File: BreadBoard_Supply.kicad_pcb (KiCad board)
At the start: 2 copper layers, 19 parts, among them J1 Barrel_Jack_Switch, J2 Selector, J3 Conn_02x02_Odd_Even, J4 Conn_02x02_Odd_Even, U1 AMS1117-5.0, U2 AMS1117-3.3

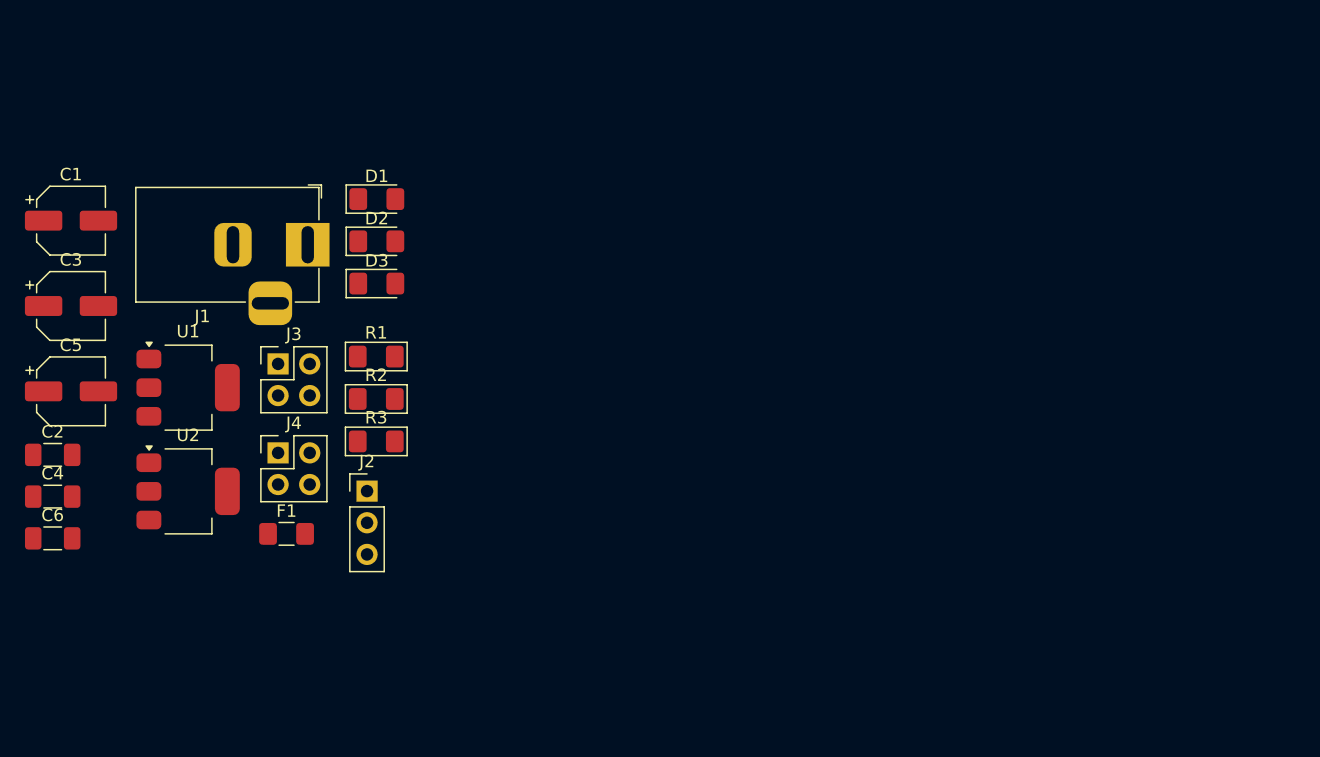
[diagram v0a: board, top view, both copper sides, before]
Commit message: Completed with DC input
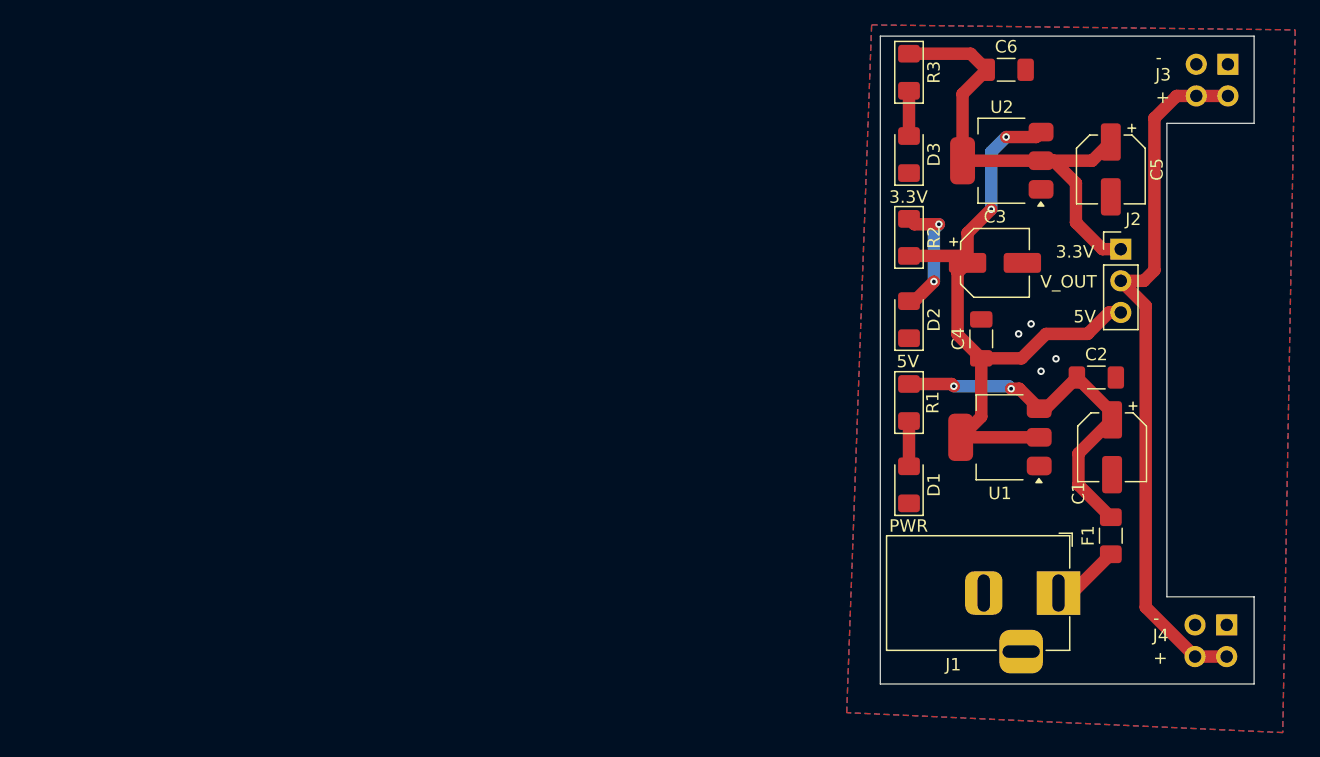
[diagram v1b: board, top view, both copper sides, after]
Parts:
- added REF**: KiCad-Logo2_5mm_SilkScreen, Symbol:KiCad-Logo2_5mm_SilkScreen, B.Cu at (205.4, 66.4)
- J3, J4: moved to B.Cu
- moved C1 85.5 mm to (211.3, 95.9), turned to -90 degrees
- moved C5 85.3 mm to (211.2, 73.6), turned to -90 degrees
- moved C6 85.3 mm to (202.8, 65.6)
- moved C2 84.0 mm to (210.0, 90.3)
- moved J3 79.9 mm to (220.6, 65.2), turned to 180 degrees
- moved J4 77.4 mm to (220.5, 110.2), turned to 180 degrees
- moved C4 75.6 mm to (200.8, 87.2), turned to 90 degrees
- moved C3 74.2 mm to (201.9, 81.1)
- moved U2 70.5 mm to (202.4, 72.9), turned to 180 degrees
- moved J1 66.4 mm to (207.0, 107.6)
- moved F1 66.2 mm to (211.2, 103.0), turned to 90 degrees
- moved U1 65.3 mm to (202.3, 95.1), turned to 180 degrees
- moved J2 63.5 mm to (212.0, 80.0)
- moved R3 52.0 mm to (195.0, 65.8), turned to -90 degrees
- moved D1 48.5 mm to (195.0, 98.9), turned to 90 degrees
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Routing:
- net /V_OUT: track 0.00 -> 57.1 mm
- net /5V: track 0.00 -> 54.1 mm, vias 0 -> 2
- net /3.3V: track 0.00 -> 38.6 mm
- net Net-(U1-VI): track 0.00 -> 29.9 mm, vias 0 -> 2
- net Net-(D2-A): track 0.00 -> 10.00 mm, vias 0 -> 2
- net Net-(F1-Pad1): track 0.00 -> 5.49 mm
- net Net-(D3-A): track 0.00 -> 3.63 mm
- net Net-(D1-A): track 0.00 -> 3.63 mm
- net GND: vias 0 -> 4
- added copper zone on B.Cu, net GND
- added copper zone on F.Cu, net GND
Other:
- board outline added: 30 x 52 mm
- board text added: "+"
- board text added: "-"
- board text added: "3.3V"
- board text added: "5V"
- board text added: "PWR"
- board text added: "V_OUT"
